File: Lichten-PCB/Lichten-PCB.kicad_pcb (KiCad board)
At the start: 2 copper layers, 54.2 x 62.2 mm, 56 parts, among them J1 Conn_01x04_Socket

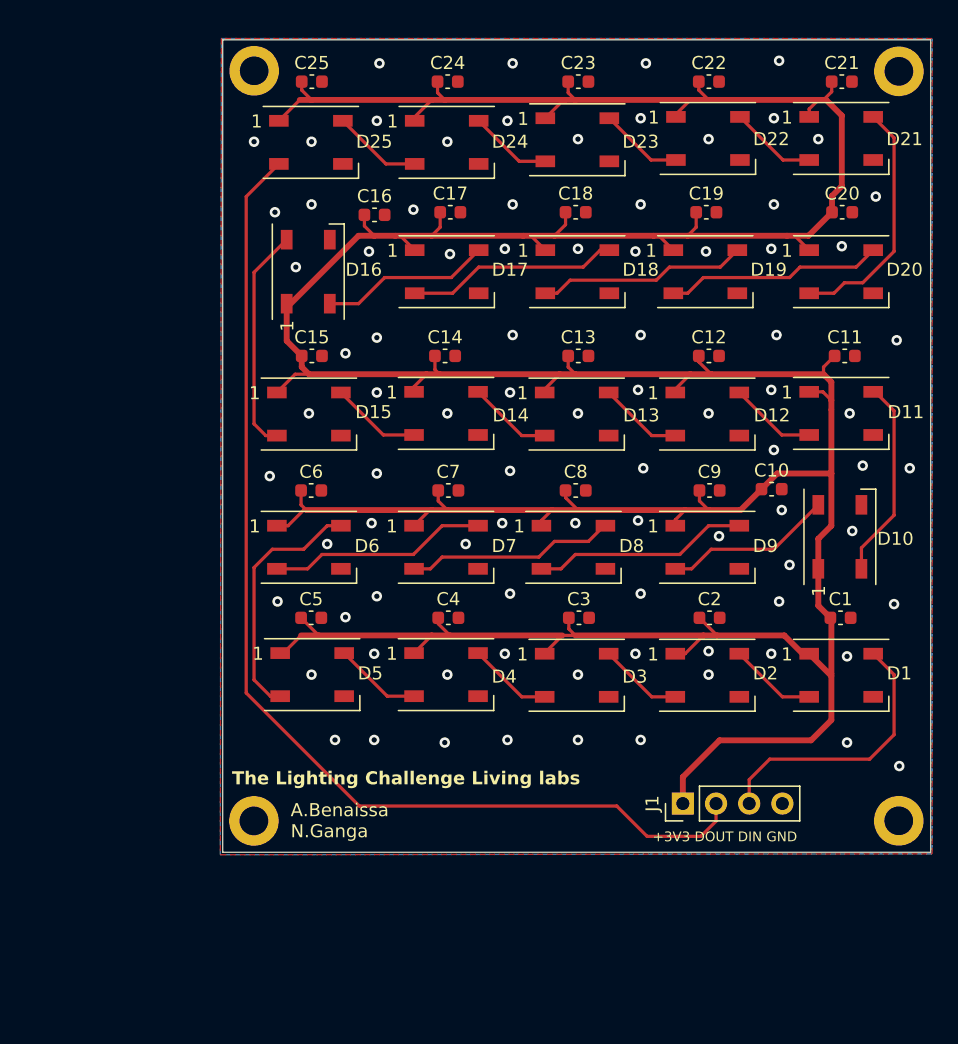
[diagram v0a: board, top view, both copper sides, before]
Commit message: Nieuwe Via aan de onderkant toegevoegd pinout back silkscreen aangemaakt en correct gespiegeld. en god said there was light goed gequote dit keer.
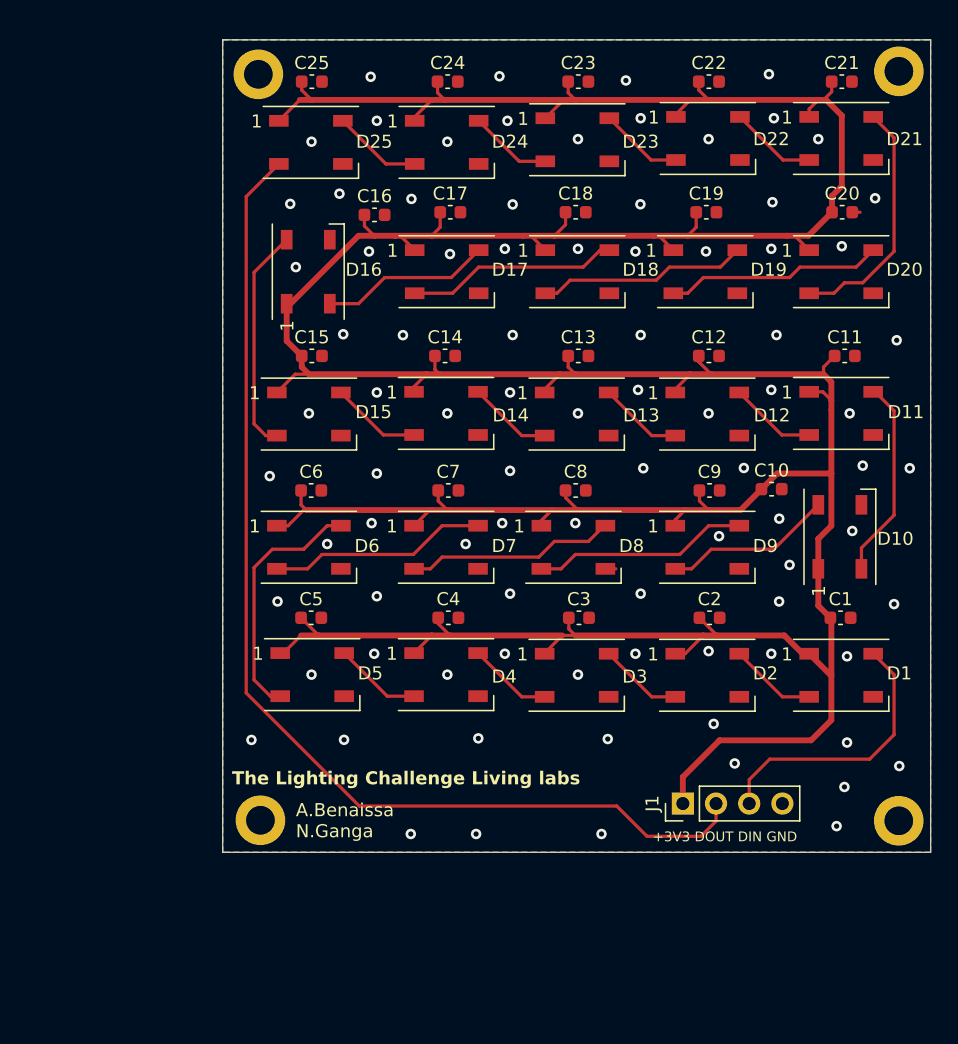
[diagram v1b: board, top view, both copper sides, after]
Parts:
- moved H3 0.50 mm to (121.1, 129.8)
- moved H2 0.42 mm to (120.9, 72.6)
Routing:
- net GND: track 0.00 -> 4.08 mm, vias 87 -> 88
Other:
- board text added: "GND DIN DOUT +3V3"
- board text added: "GOD SAID AND THERE WAS LIGHT"
- board text removed: "GOD SAID AND THERE IS LIGHT"

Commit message: Oke nu is de quote goed (hopelijjk)
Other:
- board text added: "GOD SAID LET THERE BE LIGHT"
- board text removed: "GOD SAID AND THERE WAS LIGHT"
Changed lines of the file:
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@@
     (effects (font (size 0.75 0.75) (thickness 0.12)) (justify left bottom mirror))
   )
-  (gr_text "GOD SAID AND THERE WAS LIGHT" (at 157.2 120.6) (layer "B.SilkS")
+  (gr_text "GOD SAID LET THERE BE LIGHT" (at 157.2 120.6) (layer "B.SilkS")
     (effects (font (size 1 1) (thickness 0.15)) (justify left bottom mirror))
   )

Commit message: PCB vergroot
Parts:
- added C26: 0.1u, Capacitor_SMD:C_0603_1608Metric, F.Cu at (159.8, 86.3)
- added C27: 0.1u, Capacitor_SMD:C_0603_1608Metric, F.Cu at (149.8, 86.2)
- added C28: 0.1u, Capacitor_SMD:C_0603_1608Metric, F.Cu at (140.1, 86.3)
- added C29: 0.1u, Capacitor_SMD:C_0603_1608Metric, F.Cu at (129.7, 86.3)
- added C30: 0.1u, Capacitor_SMD:C_0603_1608Metric, F.Cu at (118.3, 86.4)
- added C31: 0.1u, Capacitor_SMD:C_0603_1608Metric, F.Cu at (114.8, 86.2)
- added C32: 0.1u, Capacitor_SMD:C_0603_1608Metric, F.Cu at (118.7, 77.0)
- added C33: 0.1u, Capacitor_SMD:C_0603_1608Metric, F.Cu at (129.6, 76.4)
- added C34: 0.1u, Capacitor_SMD:C_0603_1608Metric, F.Cu at (141.3, 76.5)
- added C35: 0.1u, Capacitor_SMD:C_0603_1608Metric, F.Cu at (154.4, 76.4)
- added D26: WS2812B, LED_SMD:LED_WS2812B_PLCC4_5.0x5.0mm_P3.2mm, F.Cu at (154.8, 91.2)
- added D27: WS2812B, LED_SMD:LED_WS2812B_PLCC4_5.0x5.0mm_P3.2mm, F.Cu at (145.1, 91.2)
- added D28: WS2812B, LED_SMD:LED_WS2812B_PLCC4_5.0x5.0mm_P3.2mm, F.Cu at (134.9, 91.2)
- added D29: WS2812B, LED_SMD:LED_WS2812B_PLCC4_5.0x5.0mm_P3.2mm, F.Cu at (123.9, 91.2)
- added D30: WS2812B, LED_SMD:LED_WS2812B_PLCC4_5.0x5.0mm_P3.2mm, F.Cu at (113.2, 91.2)
- added D31: WS2812B, LED_SMD:LED_WS2812B_PLCC4_5.0x5.0mm_P3.2mm, F.Cu at (113.3, 80.2)
- added D32: WS2812B, LED_SMD:LED_WS2812B_PLCC4_5.0x5.0mm_P3.2mm, F.Cu at (123.8, 80.3)
- added D33: WS2812B, LED_SMD:LED_WS2812B_PLCC4_5.0x5.0mm_P3.2mm, F.Cu at (135.2, 80.3)
- added D34: WS2812B, LED_SMD:LED_WS2812B_PLCC4_5.0x5.0mm_P3.2mm, F.Cu at (147.7, 80.5)
- added D35: WS2812B, LED_SMD:LED_WS2812B_PLCC4_5.0x5.0mm_P3.2mm, F.Cu at (161.1, 80.5)
- moved C19 51.7 mm to (109.2, 106.8), turned to 180 degrees
- moved C20 51.5 mm to (116.0, 97.0), turned to 90 degrees
- moved D19 46.1 mm to (111.0, 100.9), turned to 90 degrees
- moved D20 43.9 mm to (123.7, 100.8)
- moved C21 43.6 mm to (129.1, 97.0), turned to 90 degrees
- moved D25 42.2 mm to (164.9, 91.2)
- moved C25 41.8 mm to (164.7, 86.5), turned to 90 degrees
- moved D18 39.5 mm to (114.2, 112.0)
- moved D21 38.0 mm to (135.5, 100.8)
- moved D24 37.7 mm to (165.2, 100.8)
- moved C18 35.4 mm to (119.3, 107.3), turned to 90 degrees
- moved C24 34.1 mm to (159.8, 97.1), turned to 90 degrees
- moved C8 29.1 mm to (119.2, 117.6), turned to 90 degrees
- moved C9 28.5 mm to (130.2, 117.6), turned to 90 degrees
- moved C11 28.3 mm to (150.0, 117.7), turned to 90 degrees
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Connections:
- net DTUS renamed DTUS1
- D25 pad 2: DOUT -> DTUS2
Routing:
- net +3V3: track 348.3 -> 445.0 mm
- net /LED's/Data-33: track 0.00 -> 19.7 mm
- net /LED's/Data-32: track 0.00 -> 18.7 mm
- net /LED's/Data-31: track 0.00 -> 17.7 mm
- net /LED's/Data-29: track 0.00 -> 17.4 mm
- net /LED's/Data-30: track 0.00 -> 12.9 mm
- net /LED's/Data-24: track 6.87 -> 19.3 mm
- net /LED's/Data-5: track 19.1 -> 6.67 mm
- net /LED's/Data-15: track 17.3 -> 6.40 mm
- net /LED's/Data-23: track 6.38 -> 16.8 mm
- net /LED's/Data-17: track 16.3 -> 6.87 mm
- net /LED's/Data-22: track 6.43 -> 15.8 mm
- net /LED's/Data-21: track 6.67 -> 15.9 mm
- net /LED's/Data-27: track 0.00 -> 7.54 mm
- net /LED's/Data-28: track 0.00 -> 7.22 mm
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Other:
- board size 54.2 x 62.2 mm -> 69.2 x 75.8 mm
- board text added: "D6"

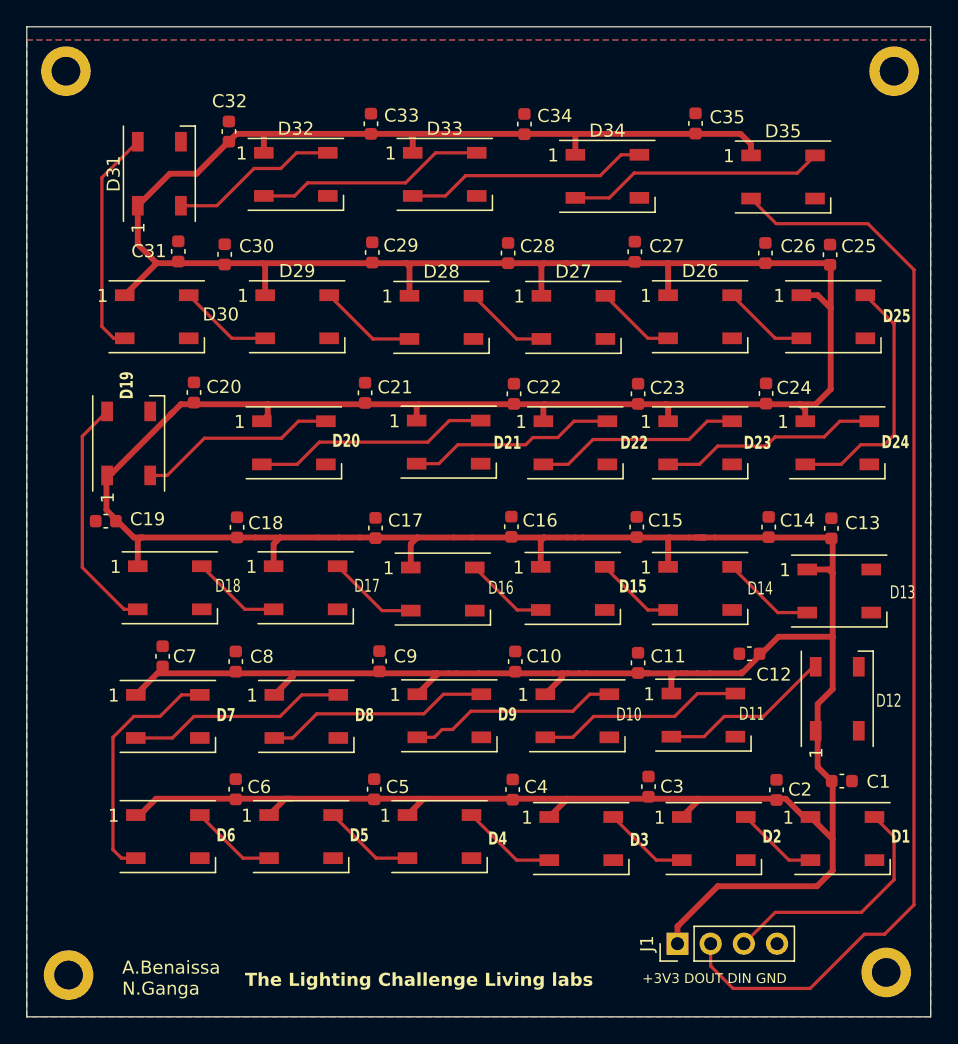
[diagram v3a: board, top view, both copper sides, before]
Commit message: Trace dikte aangepast naar 0.667 mm
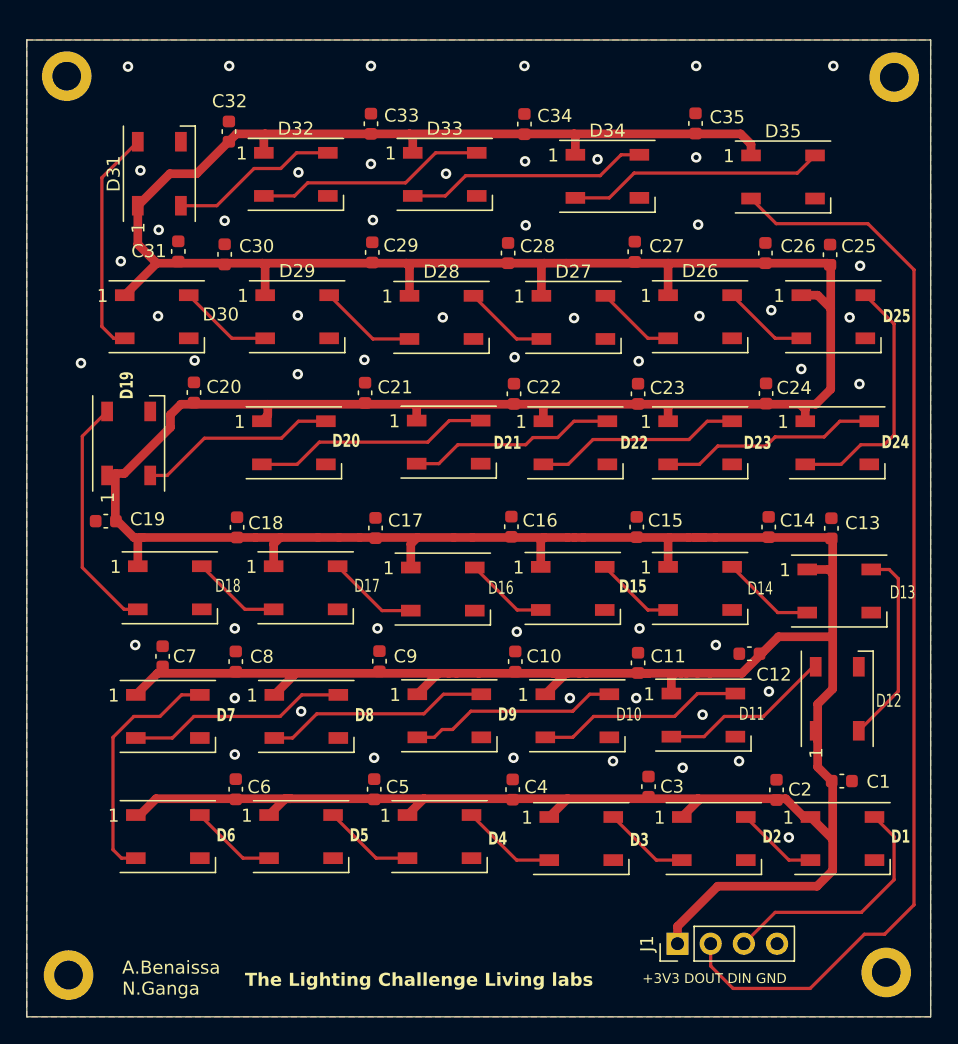
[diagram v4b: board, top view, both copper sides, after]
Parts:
- moved G*** 2.93 mm to (138.4, 102.4)
- moved H1 0.46 mm to (169.6, 72.9)
- moved H2 0.38 mm to (106.3, 72.8)
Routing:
- net /LED's/Data-12: track 0.00 -> 15.3 mm
- net +3V3: track 445.0 -> 444.0 mm
- net GND: vias 0 -> 54
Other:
- board size 69.2 x 75.8 mm -> 69.2 x 74.8 mm

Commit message: Footprint van connector aangepast
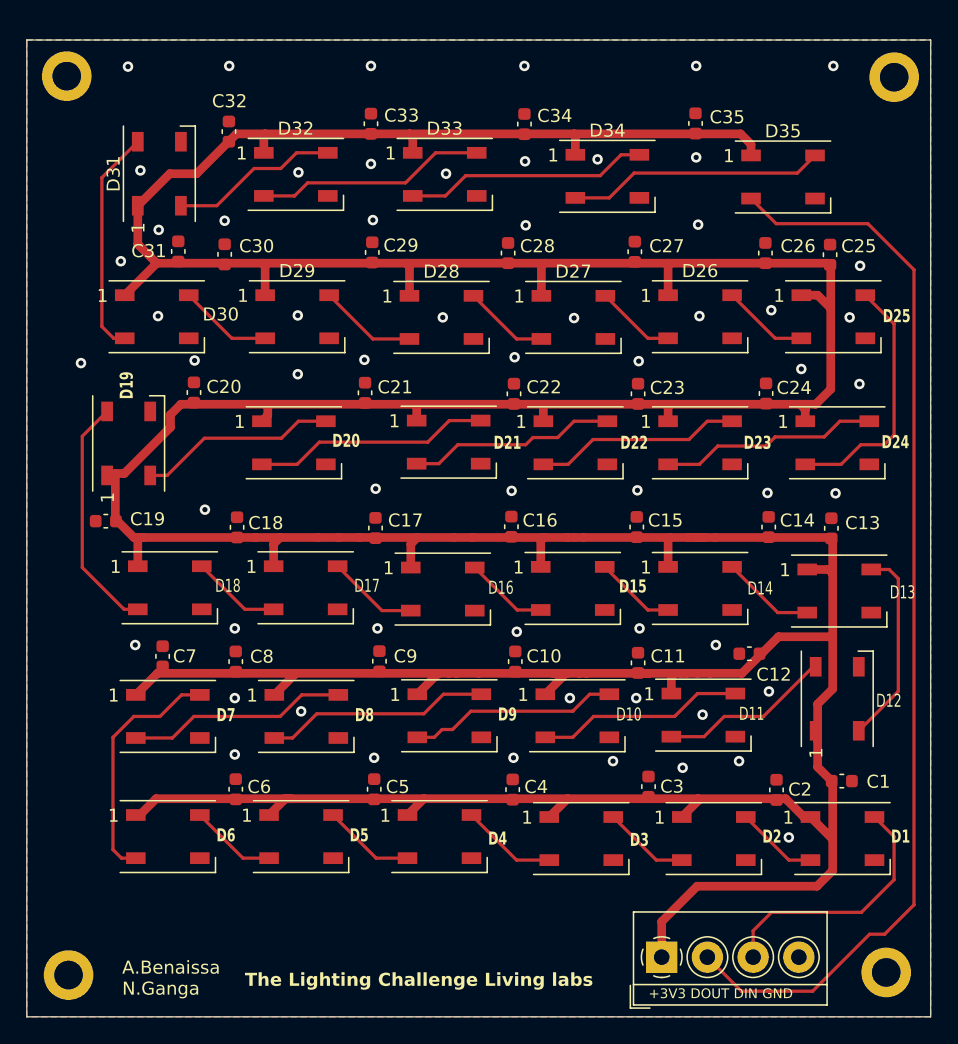
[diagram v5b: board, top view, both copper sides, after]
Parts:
- J1: footprint Connector_PinHeader_2.54mm:PinHeader_1x04_P2.54mm_Vertical -> TerminalBlock_4Ucon:TerminalBlock_4Ucon_1x04_P3.50mm_Horizontal
- moved J1 1.59 mm to (151.8, 140.2), turned to 0 degrees
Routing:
- net +3V3: track 444.0 -> 446.4 mm
- net DOUT: track 84.0 -> 83.0 mm
- net DIN: track 19.0 -> 19.9 mm
- net GND: vias 54 -> 60

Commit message: Via's geplaatst en DOUT gereroute
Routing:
- net DOUT: track 83.0 -> 81.9 mm
- net /LED's/Data-24: track 19.3 -> 18.5 mm
- net GND: vias 60 -> 121
